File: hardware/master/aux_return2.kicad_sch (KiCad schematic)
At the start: 98 parts, among them J301 RETURN 2 L/MONO, J302 RETURN 2 R, J303 GAIN: fitted -6 dB (PRO), ope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, SW301 RETURN 2 MUTE (latching), SW302 RETURN 2 DUCK (latching), SW303 RETURN 2 COMP (latching), U301 AD8273, U302 NE5532, U303 SSI2162, U304 NE5532, U305 NE5532, U306 TL072, U307 TL072, U308 DG413DY, U309 DG413DY

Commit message: Master card: draw decisions 97 and 98, OPA2171 fader-law stages (103), SC_ENV drive (104)
- AUX returns: SC_ENV into the summer's virtual earth through R232/R332 30k1,
  R233/R333 removed, summer + input on AGND (decision 97)
- Q501 emitter and button pull-downs R237/239/241, R337/339/341, R455,
  R523/525/527 to PGND (decision 98)
- U206, U306, U705 = OPA2171 for the pot buffer and control summer; superdiodes
  on the TL072s U207, U307, U706 (decision 103)
- Sidechain: DEPTH negative (R518 to -15 V), U505B follower fed back after R521,
  D504 BAT54T1G clamp to AGND (decision 104); simulation rerun with 1.7 kOhm load
- R421 on its 0603 footprint (system validation finding 3)
- Power budget, parts list, STATUS, decisions and working notes updated

Co-Authored-By: Claude Opus 5.5 <noreply@anthropic.com>
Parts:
- removed R333: 15k8, Resistor_SMD:R_0805_2012Metric, symbol Device:R
- removed U306: TL072, Package_SO:SOIC-8_3.9x4.9mm_P1.27mm, symbol Amplifier_Operational:TL072
- added U306: OPA2171, Package_SO:SOIC-8_3.9x4.9mm_P1.27mm, symbol Amplifier_Operational:Opamp_Dual
- R332: value 100k -> 30k1; Note (none) -> SC_ENV into the virtual earth: 0.332 V/V, 10 dB of ducking 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; ProjectPN SX-R-007 -> SX-R-087
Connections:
- net +15V: now also U306.8 (V+)
- net -15V: now also U306.4 (V-)
- net AGND: now also U306.5 (+); no longer R337.1, R339.1, R341.1
- net PGND: now also R337.1, R339.1, R341.1
- net VC: now also U306.7; no longer U307.7
- net at C315.1, R322.2, R323.2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: now also R332.2, U306.6 (-); no longer U307.6 (-)
- net at R322.1, R324.1, R327.1: now also U306.1, U306.2 (-)
- net DUCK_V: now reaches R332.1, U308.2
- net at R324.2, R325.2: now also U307.5 (+)
- net at D301.2 (A), R326.1: now also U307.6 (-)
- net at D301.1 (K): now also U307.7
- net at RV301.2: now also U306.3 (+)
- removed net VPLUS: R332.2, U307.5 (+)

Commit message: Master card: DRV135 outputs, TL062 levers, SMD electrolytics, both raw rails watched (decisions 125-128)
/board master pre-layout session; the user delegated the open points.
- Confirms the [proposed] parts of decisions 89-94 (Q5 checked, +22 dB
  makeup kept for the breadboard, fallback R439 = 330k).
- 125: TI DRV135UA replaces the end-of-life THAT1646 (THAT memo
  2026-09-01); same SO-8 pinout, LCSC C544663.
- 126: U409, U410, U802, U804 TL072 -> TL062; superdiodes and U407 stay.
- 127: master electrolytics to SMD (decision 111 parts, 5.4 mm).
- 128: U707C watches -20V_RAW (22k6/100k), wired-OR with the +20 V trip.
- Würth fields on J101/J901, BAT54 LCSC C152458, G6K and header
  drawings checked, LCSC stock checked; budget 331/260 mA typical.
- parts.csv candidates for master pots and meter LEDs; lcsc_check.py
  handles MOhm.
ERC 0/0, all netlist checks 0 problems, reuse lint clean.

Co-Authored-By: Claude Opus 5.5 <noreply@anthropic.com>
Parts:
- C305, C306, C309, C310: footprint Capacitor_THT:C_Radial_D5.0mm_H11.0mm_P2.00mm -> Capacitor_SMD:C_Elec_6.3x5.4; MPN (none) -> EEE-1VA100NP; Manufacturer (none) -> Panasonic; ProjectPN SX-C-003 -> SX-C-023; Supplier (none) -> Mouser; SupplierPN (none) -> 667-EEE-1VA100NP

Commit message: System: cost review and cost control (decisions 132-137)
Rean NYS216 jacks with a new footprint (132), through-hole parts hand-soldered (133), E24 values owned per board (134), live-device cost principle (135), /cost with the cost-controller sub-agent, tools/costs.py and a private ledger of realized costs (136), JLCPCB fee-free parts first (137).

Co-Authored-By: Claude Opus 5.5 <noreply@anthropic.com>
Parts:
- J301, J302: footprint Connector_Audio:Jack_6.35mm_Neutrik_NMJ6HCD2_Horizontal -> syntsamix:Jack_6.35mm_Rean_NYS216_Horizontal; MPN NMJ6HCD2 -> NYS216; Manufacturer Neutrik -> Rean; ProjectPN SX-CONN-001 -> SX-CONN-015
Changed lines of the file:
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@@
 			)
 		)
-		(property "Footprint" "Connector_Audio:Jack_6.35mm_Neutrik_NMJ6HCD2_Horizontal"
+		(property "Footprint" "syntsamix:Jack_6.35mm_Rean_NYS216_Horizontal"
 			(at 30.48 50.8 0)
 			(hide yes)
@@
 			)
 		)
-		(property "ProjectPN" "SX-CONN-001"
+		(property "ProjectPN" "SX-CONN-015"
 			(at 30.48 50.8 0)
 			(hide yes)
@@
 			)
 		)
-		(property "Manufacturer" "Neutrik"
+		(property "Manufacturer" "Rean"
 			(at 30.48 50.8 0)
 			(hide yes)
@@
 			)
 		)
-		(property "MPN" "NMJ6HCD2"
+		(property "MPN" "NYS216"
 			(at 30.48 50.8 0)
 			(hide yes)
@@
 			)
 		)
-		(property "Footprint" "Connector_Audio:Jack_6.35mm_Neutrik_NMJ6HCD2_Horizontal"
+		(property "Footprint" "syntsamix:Jack_6.35mm_Rean_NYS216_Horizontal"
 			(at 30.48 76.2 0)
 			(hide yes)
@@
 			)
 		)
-		(property "ProjectPN" "SX-CONN-001"
+		(property "ProjectPN" "SX-CONN-015"
 			(at 30.48 76.2 0)
 			(hide yes)
@@
 			)
 		)
-		(property "Manufacturer" "Neutrik"
+		(property "Manufacturer" "Rean"
 			(at 30.48 76.2 0)
 			(hide yes)
@@
 			)
 		)
-		(property "MPN" "NMJ6HCD2"
+		(property "MPN" "NYS216"
 			(at 30.48 76.2 0)
 			(hide yes)

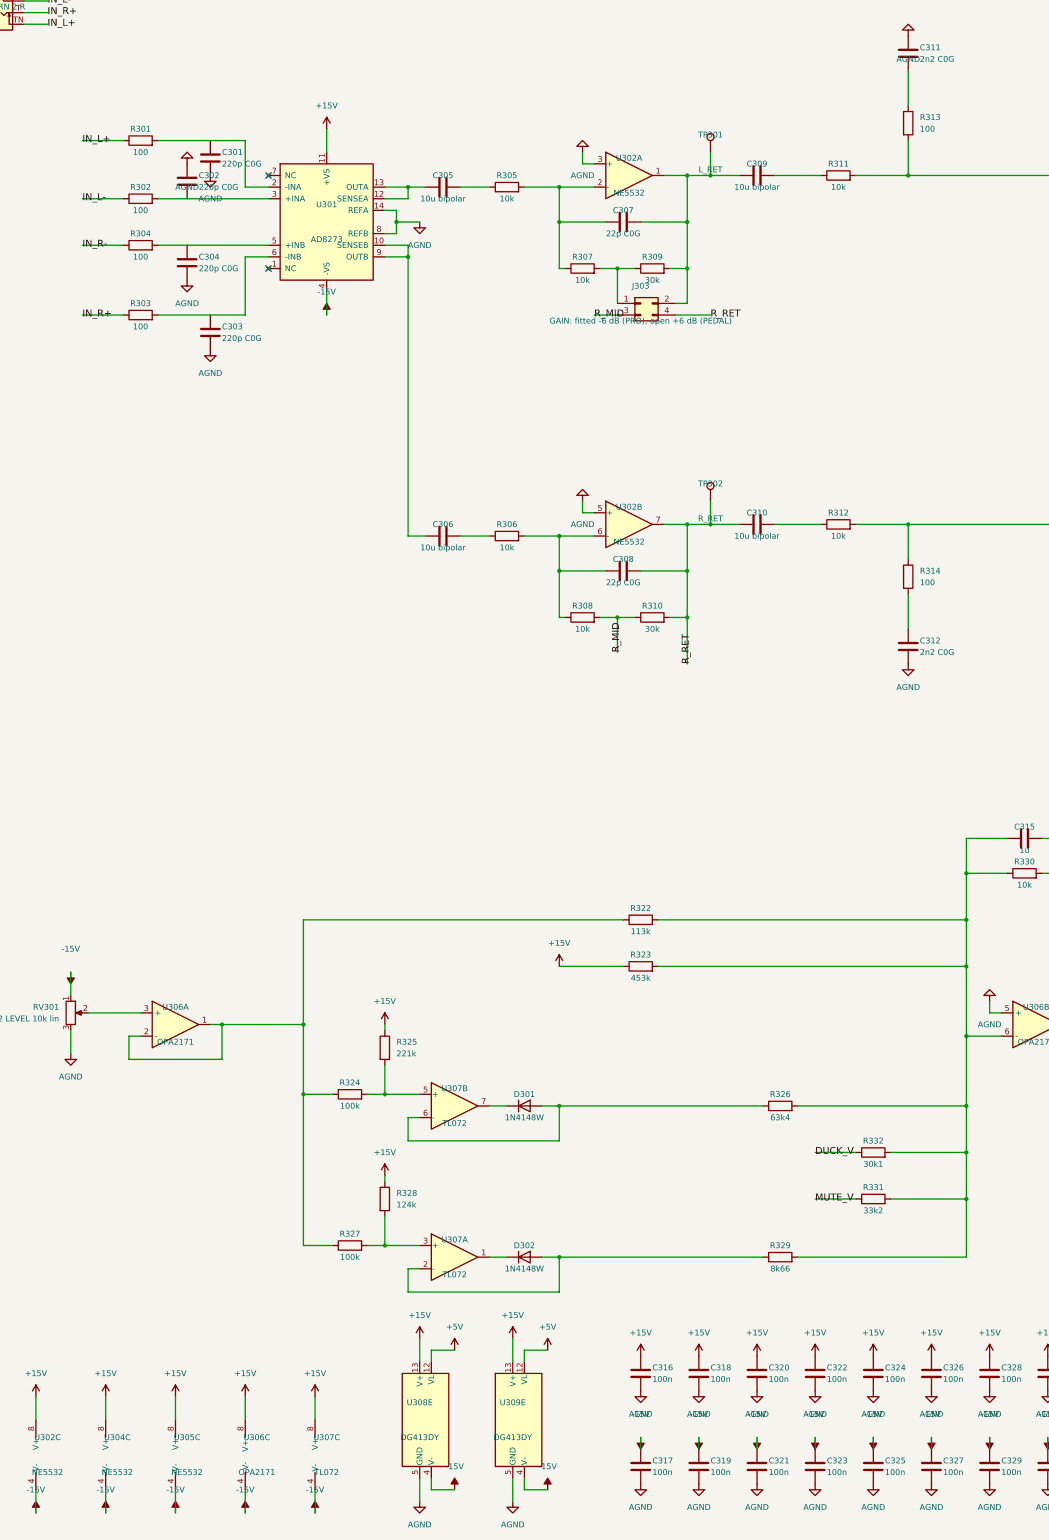
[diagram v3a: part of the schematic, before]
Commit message: Master card: fee-free parts and E24 values (decisions 144, 146-150)
- 144: AUX return and master fader laws on the channel's E24 pairs
- 146: meter ladder on fee-free E24 values (0.45 mA, within 0.14 dB); R732 22k + R737 560R
- 147: compressor R420/R426 E24 pairs, GR LED ladder 470k/4k3, SC LPF C503 2 x 47n C0G
  (Q 0.707, 44-478 Hz); TL072 symbols ST TL072CDT
- 148: AUX return receivers TL072 difference amplifiers (AD8273 gone from the project)
- 149: R421 plain 1k; compressor temperature compensation to the backlog
- 150: DG413, SSI2162, DRV135UA, AS3046D hand-soldered on the prototype master
  (symbol field Assembly, read by tools/costs.py); SPOF noted in the backlog
- Part swaps: button LEDs per colour, D504 BAT54W, D705-D712 1N4007W SOD-123FL,
  U641 DG411 -> DG413 with a Q601 inverter for send 1 (emitter on PGND, invariant 4)
- 70 -> 38 extended/consigned SMD types (about EUR 193 -> 105 per order);
  estimate EUR 794 / 1,074 / 1,671 for 4 / 8 / 16 channels
- Docs: STATUS, CONTINUE-FROM-HERE, ROADMAP backlog, SPEC, hardware/CLAUDE.md lessons

Co-Authored-By: Claude Opus 5.5 <noreply@anthropic.com>
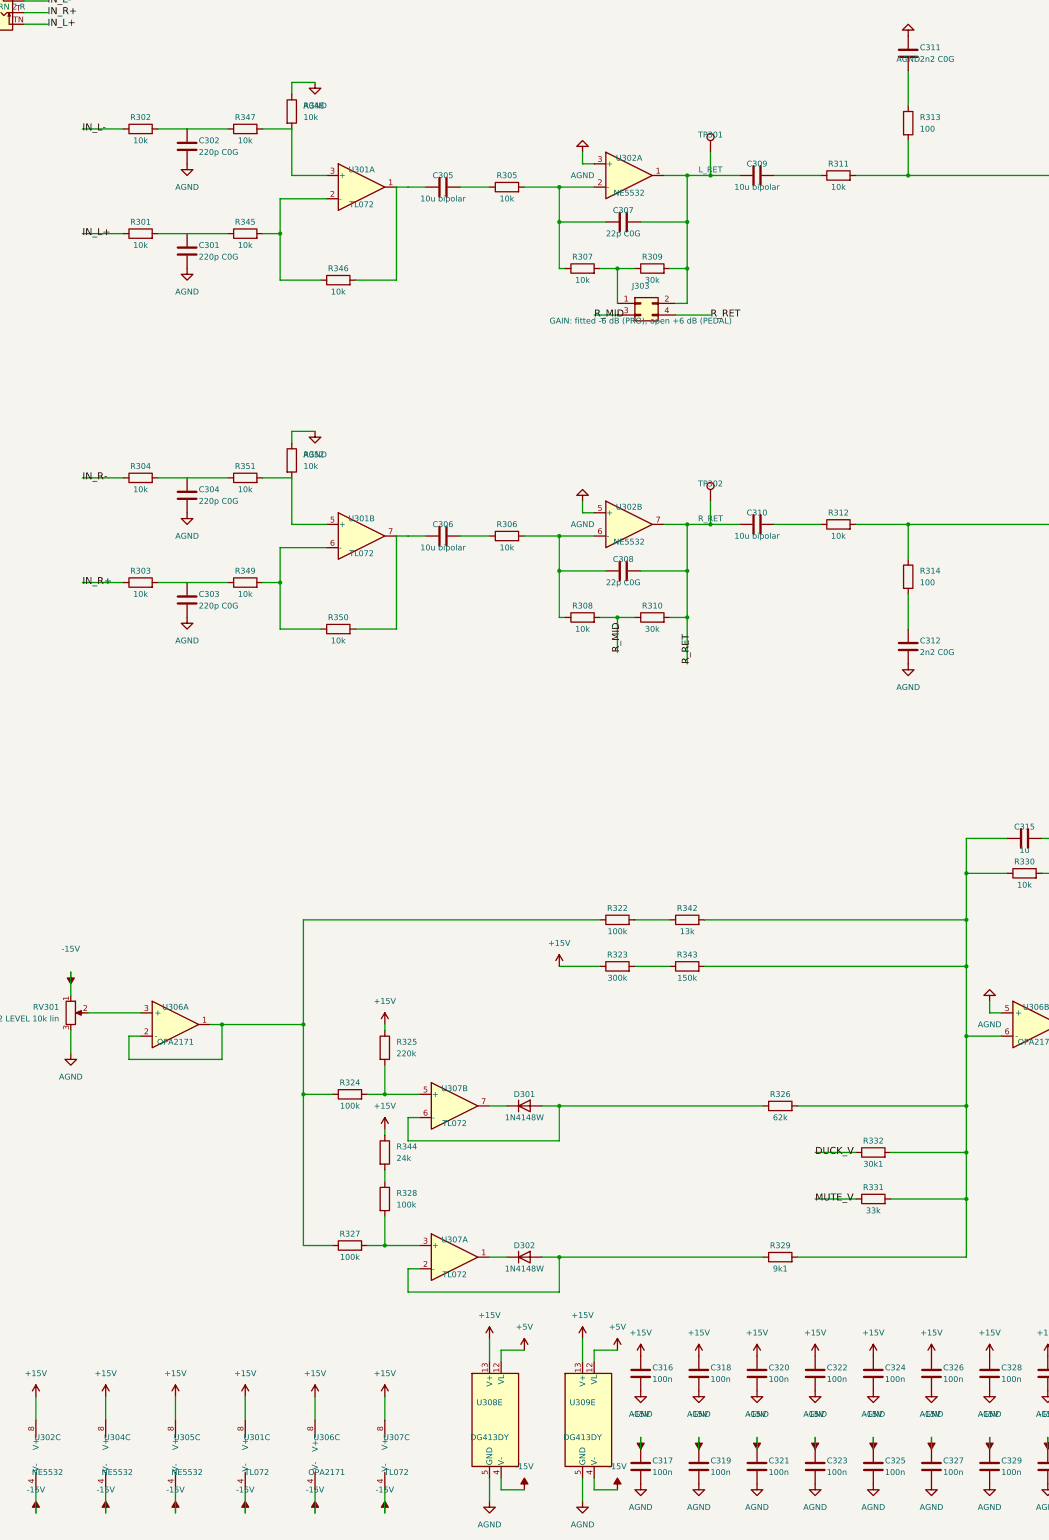
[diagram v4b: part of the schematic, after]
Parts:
- removed U301: AD8273, Package_SO:SOIC-14_3.9x8.7mm_P1.27mm, symbol syntsamix:AD8273
- added R342: 13k, Resistor_SMD:R_0805_2012Metric, symbol Device:R
- added R343: 150k, Resistor_SMD:R_0805_2012Metric, symbol Device:R
- added R344: 24k, Resistor_SMD:R_0805_2012Metric, symbol Device:R
- added R345, R346, R347, R348, R349, R350, R351, R352: 10k, Resistor_SMD:R_0805_2012Metric, symbol Device:R
- added U301: TL072, Package_SO:SOIC-8_3.9x4.9mm_P1.27mm, symbol Amplifier_Operational:TL072
- D303: MPN (none) -> NCD0805R1; Manufacturer (none) -> Foshan NationStar; ProjectPN SX-D-002 -> SX-D-015; Supplier (none) -> LCSC; SupplierPN (none) -> C84256
- D304, D305: MPN (none) -> KT-0805G; Manufacturer (none) -> Hubei KENTO; ProjectPN SX-D-002 -> SX-D-011; Supplier (none) -> LCSC; SupplierPN (none) -> C2297
- R301, R302, R303, R304: value 100 -> 10k; MPN (none) -> RT0805BRD0710KL; Manufacturer (none) -> YAGEO; Note (none) -> 0.1 %: receiver resistor match sets the CMRR (decision 148); ProjectPN SX-R-001 -> SX-R-107; Supplier (none) -> LCSC; SupplierPN (none) -> C110775
- R322: value 113k -> 100k; ProjectPN SX-R-023 -> SX-R-007
- R323: value 453k -> 300k; ProjectPN SX-R-024 -> SX-R-096
- R325: value 221k -> 220k; ProjectPN SX-R-025 -> SX-R-103
- R326: value 63k4 -> 62k; ProjectPN SX-R-026 -> SX-R-102
- R328: value 124k -> 100k; ProjectPN SX-R-027 -> SX-R-007
- R329: value 8k66 -> 9k1; ProjectPN SX-R-014 -> SX-R-095
- R331: value 33k2 -> 33k; ProjectPN SX-R-028 -> SX-R-006
- U303, U308, U309: Assembly (none) -> hand (decision 150)
- U307: MPN (none) -> TL072CDT; Manufacturer Texas Instruments -> STMicroelectronics; Supplier (none) -> LCSC; SupplierPN (none) -> C6961
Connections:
- net +15V: now also R344.1, U301.8 (V+); no longer R328.1
- net -15V: now also U301.4 (V-)
- net AGND: now also R348.1, R352.1
- net at C303.1, R303.2: now also R349.1
- net at C306.1: now also R350.2, U301.7
- net at C305.1: now also R346.2, U301.1
- net at C301.1, R301.2: now also R345.1
- net at C302.1, R302.2: now also R347.1
- net at C304.1, R304.2: now also R351.1
- net at C315.1, R326.2, R329.2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: now also R342.2, R343.2; no longer R322.2, R323.2
- new net: R328.1, R344.2
- new net: R351.2, R352.2, U301.5 (+)
- new net: R349.2, R350.1, U301.6 (-)
- new net: R323.2, R343.1
- new net: R347.2, R348.2, U301.3 (+)
- new net: R345.2, R346.1, U301.2 (-)
- new net: R322.2, R342.1
- no-connect marks 12 -> 10

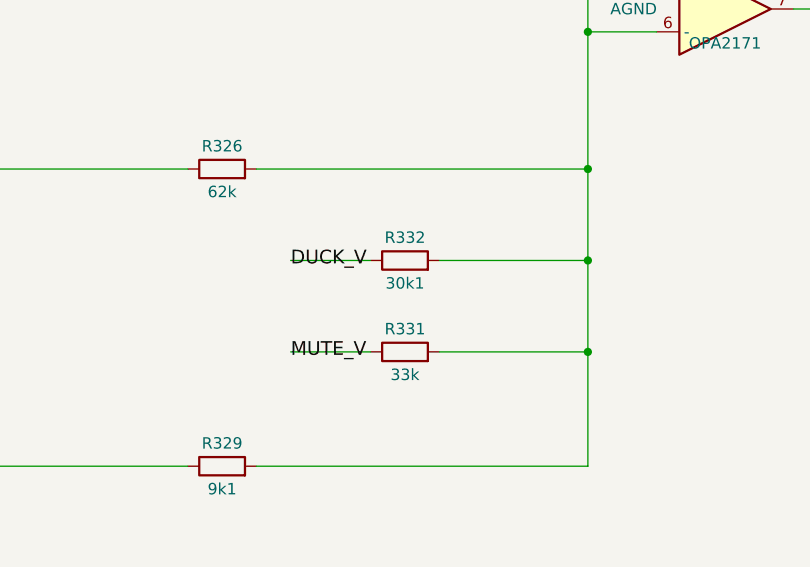
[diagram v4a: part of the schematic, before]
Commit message: Master card: R232/R332 30k (decision 153)
AUX return sheets: R232/R332 30k1 -> 30k (SX-R-050, JLCPCB basic);
SX-R-087 no longer used. simulation/sidechain load 18 x 30k = 1.667 kOhm,
results unchanged. Netlists match (73 nets each), ERC 0/0. Cost: 35 fee
types, EUR 785/1,066/1,663 for 4/8/16 channels. STATUS.md trimmed;
drawn part swaps moved to CHECKLISTS.md.

Co-Authored-By: Claude Opus 5.5 <noreply@anthropic.com>
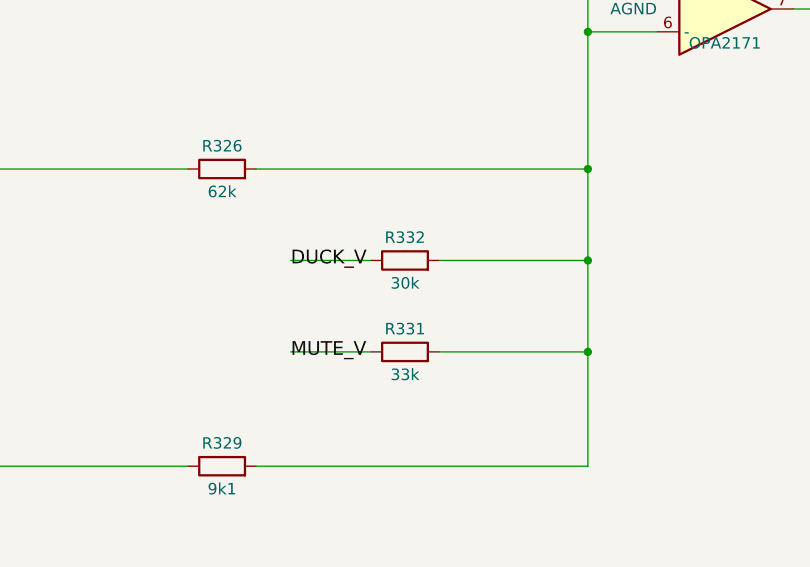
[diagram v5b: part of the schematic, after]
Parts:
- R332: value 30k1 -> 30k; Note SC_ENV into the virtual earth: 0.332 V/V, 10 dB of ducking 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 -> SC_ENV into the virtual earth: 0.333 V/V, 10 dB of ducking 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; ProjectPN SX-R-087 -> SX-R-050

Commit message: Buttons: SX-SW-001 is the latching GPBS850L, not the momentary GPBS850N
Electrokit 41012905 (on-on, latching) links the GPBS850N datasheet, which
is the momentary twin (Electrokit 41015527, Mouser "Non-Latching ON-(ON)");
the MPN was copied from that file. The latching part is CW GPBS850L
(datasheet Rev 2, 2014: same body, pin grid and pressed = 2-3, 5-6 contacts;
plunger 4.0 mm instead of 3.8).

MPN and footprint name corrected on all 17 button symbols, the generator
scripts and the input reference; parts.csv gets the GPBS850L datasheet and
RoHS source (Mouser 629-GPBS-850L, DigiKey CW179-ND); prices.csv gets the
Electrokit price (6.48 SEK ex VAT at 25+). Erratum on decision 75, checklist
item for the delivered switches and cap sizing, correction notes in the
RoHS audit and the cost review. No wiring change; ERC 0/0 on both cards.
Estimate €769 / €1,037 / €1,609 for 4 / 8 / 16 channels.

Co-Authored-By: Claude Opus 5.5 <noreply@anthropic.com>
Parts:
- SW301, SW302, SW303: footprint syntsamix:SW_Latching_8.5x8.5mm_CW_GPBS850N -> syntsamix:SW_Latching_8.5x8.5mm_CW_GPBS850L; MPN GPBS850N -> GPBS850L
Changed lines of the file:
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@@
 			)
 		)
-		(property "Footprint" "syntsamix:SW_Latching_8.5x8.5mm_CW_GPBS850N"
+		(property "Footprint" "syntsamix:SW_Latching_8.5x8.5mm_CW_GPBS850L"
 			(at 421.64 289.56 0)
 			(hide yes)
@@
 			)
 		)
-		(property "MPN" "GPBS850N"
+		(property "MPN" "GPBS850L"
 			(at 421.64 289.56 0)
 			(hide yes)
@@
 			)
 		)
-		(property "Footprint" "syntsamix:SW_Latching_8.5x8.5mm_CW_GPBS850N"
+		(property "Footprint" "syntsamix:SW_Latching_8.5x8.5mm_CW_GPBS850L"
 			(at 421.64 350.52 0)
 			(hide yes)
@@
 			)
 		)
-		(property "MPN" "GPBS850N"
+		(property "MPN" "GPBS850L"
 			(at 421.64 350.52 0)
 			(hide yes)
@@
 			)
 		)
-		(property "Footprint" "syntsamix:SW_Latching_8.5x8.5mm_CW_GPBS850N"
+		(property "Footprint" "syntsamix:SW_Latching_8.5x8.5mm_CW_GPBS850L"
 			(at 421.64 320.04 0)
 			(hide yes)
@@
 			)
 		)
-		(property "MPN" "GPBS850N"
+		(property "MPN" "GPBS850L"
 			(at 421.64 320.04 0)
 			(hide yes)
